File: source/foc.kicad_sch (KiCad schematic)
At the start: 27 parts, among them J1 Conn_01x03, J2 Conn_01x04_Male, J3 Conn_01x05, SW1 SW_DPDT_x2, U1 TJA1050T/CM,118

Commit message: jlcpcb order
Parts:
- added C5, C6: 100n, Capacitor_SMD:C_0603_1608Metric, symbol BLDC_4-rescue:C-RESCUE-BLDC_4
- added H1, H2: MountingHole, MountingHole:MountingHole_2mm, symbol Mechanical:MountingHole
- added R7, R8: 1k, Resistor_SMD:R_0603_1608Metric, symbol BLDC_4-rescue:R-RESCUE-BLDC_4
- added U2: BMI160, Package_LGA:Bosch_LGA-14_3x2.5mm_P0.5mm, symbol Cheap-FOCer-2-60mm-rescue:BMI160-IMU
- renumbered H8 to H10, H9 to H11, H10 to H12, H11 to H13, H12 to H14, H1 to H3, H2 to H4, H3 to H5, H4 to H6, H5 to H7, H6 to H8, H7 to H9
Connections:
- net GND: now also C5.1, C6.1, U2.1 (SDO), U2.6 (GNDIO), U2.7 (GND)
- net VCC: now also C5.2, C6.2, R7.2, R8.1, U2.12 (CSB), U2.5 (VDDIO), U2.8 (VDD)
- new net mcu/PA15: R8.2, U2.13 (SCX)
- new net mcu/PB2: R7.1, U2.14 (SDX)
- no-connect marks 9 -> 15
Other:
- sheet mcu ports: added PA15, PB2; removed none

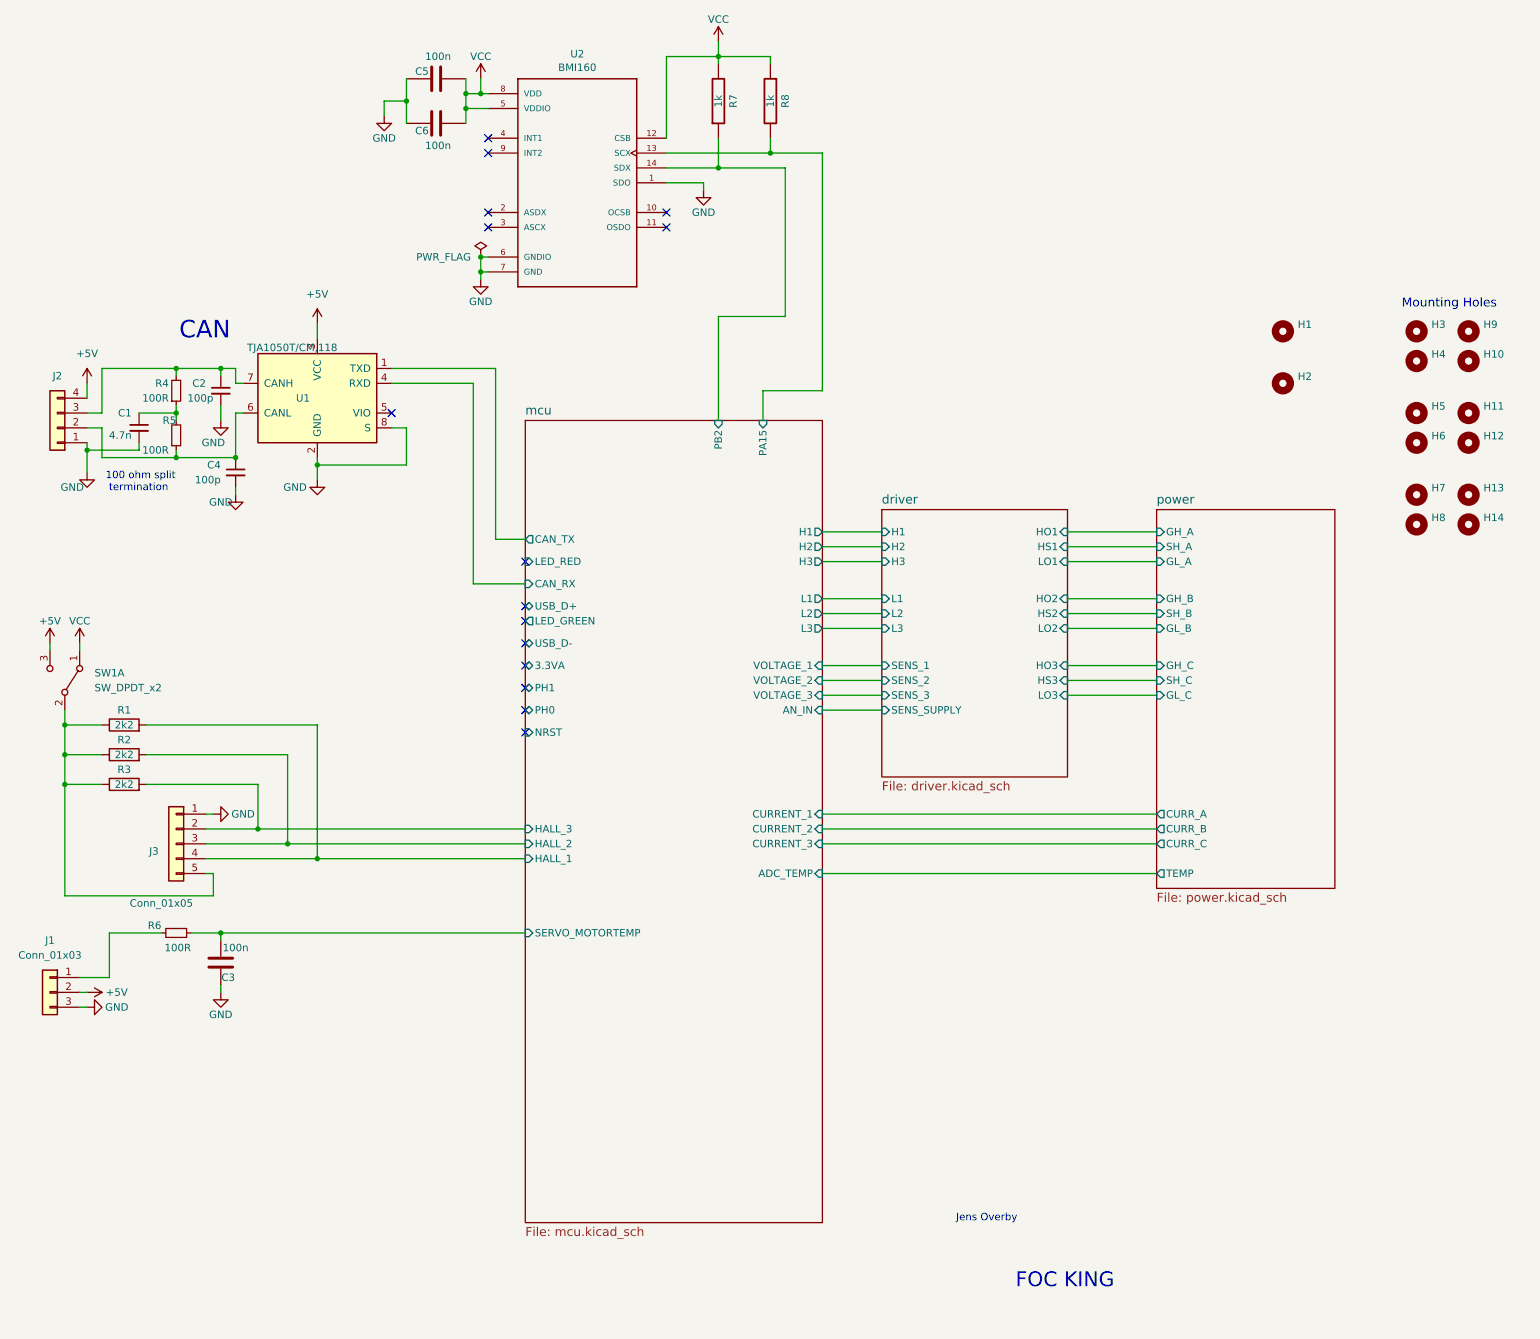
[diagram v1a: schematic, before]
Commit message: jlcpcb reorder of main-module only
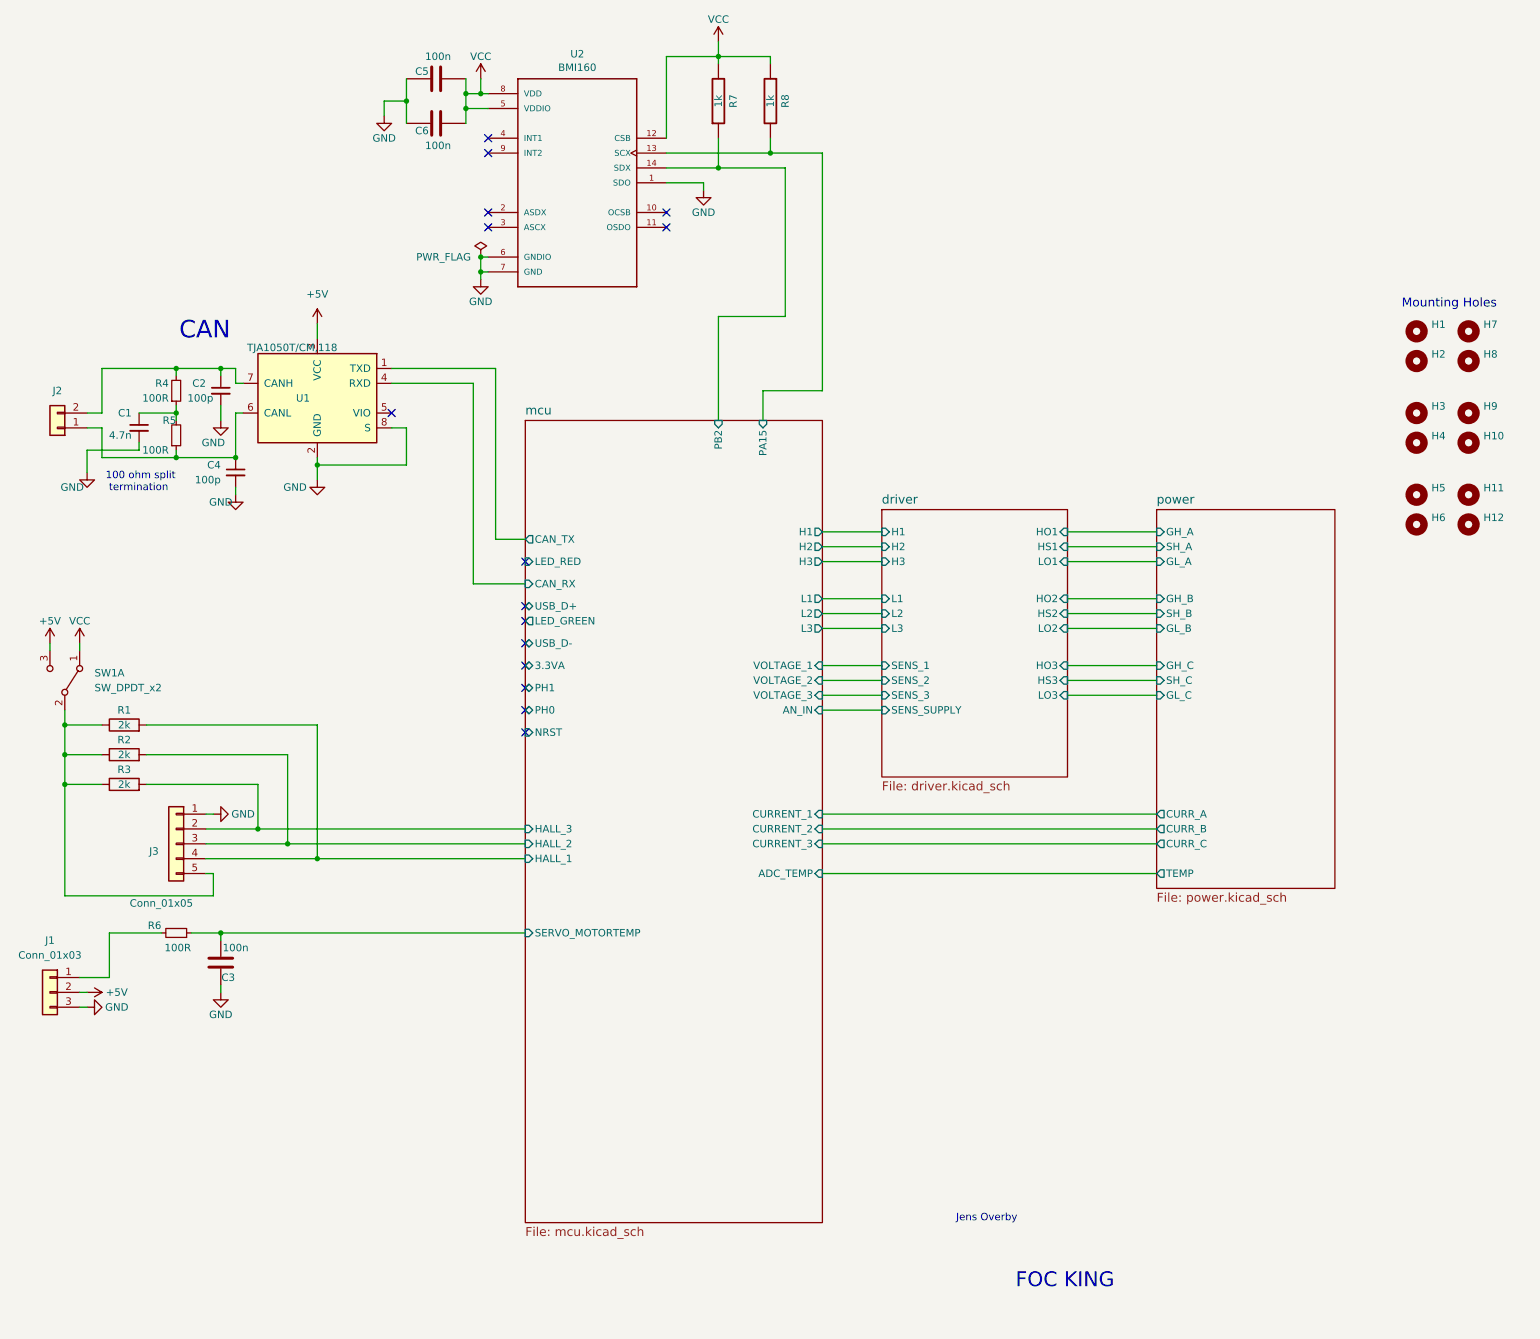
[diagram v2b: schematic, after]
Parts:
- removed H1, H2: MountingHole, MountingHole:MountingHole_2mm, symbol Mechanical:MountingHole
- C3: footprint Resistor_SMD:R_0603_1608Metric -> Capacitor_SMD:C_0603_1608Metric
- J2: footprint Connector_JST:JST_PH_B4B-PH-K_1x04_P2.00mm_Vertical -> Connector_JST:JST_PH_B2B-PH-K_1x02_P2.00mm_Vertical; symbol Connector_Generic:Conn_01x04 -> Connector_Generic:Conn_01x02
- R1, R2, R3: value 2k2 -> 2k
- renumbered H3 to H1, H12 to H10, H13 to H11, H14 to H12, H4 to H2, H5 to H3, H6 to H4, H7 to H5, H8 to H6, H9 to H7, H10 to H8, H11 to H9
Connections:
- net +5V: no longer J2.4 (Pin_4)
- net GND: no longer J2.1 (Pin_1)
- net at C2.1, R4.2, U1.7 (CANH): now also J2.2 (Pin_2); no longer J2.3 (Pin_3)
- net at C4.1, R5.1, U1.6 (CANL): now also J2.1 (Pin_1); no longer J2.2 (Pin_2)

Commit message: Add files via upload
Added six pull down resistors to mosfet gates, and removed 100 pF filter caps on current samplings. Changed Logo back to FOC-king. This is a potential release candidates - everything works, also HFI. Have not yet verified NRF though.
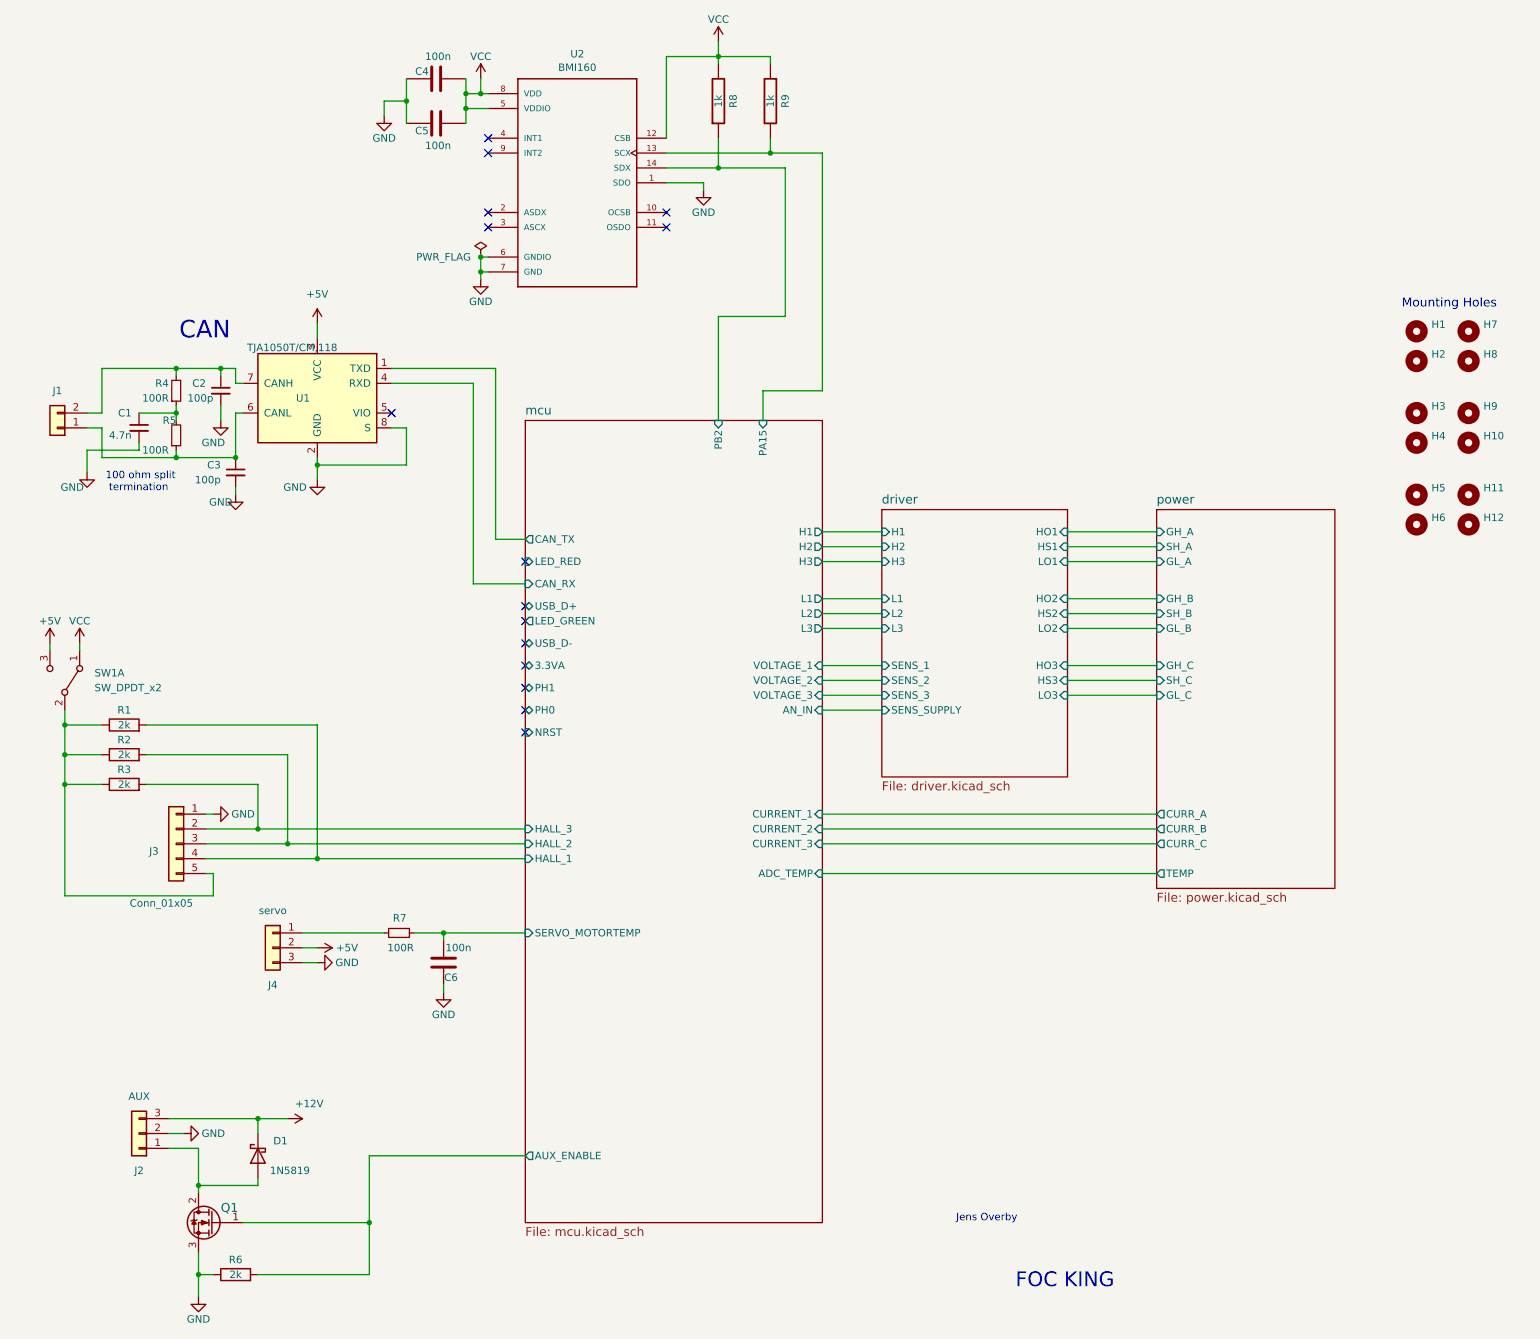
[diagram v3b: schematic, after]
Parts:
- added D1: 1N5819, Diode_SMD:D_SOD-323, symbol Diode:1N5819
- added J2: AUX, Connector_JST:JST_PH_B3B-PH-K_1x03_P2.00mm_Vertical, symbol Connector_Generic:Conn_01x03
- added Q1: AO3400A, Package_TO_SOT_SMD:SOT-23, symbol Device:Q_NMOS_GDS
- added R6: 2k, Resistor_SMD:R_0603_1608Metric, symbol Device:R
- J4: renamed from J1; value Conn_01x03 -> servo
- renumbered C4 to C3, C5 to C4, C6 to C5, C3 to C6, J2 to J1, R6 to R7, R7 to R8, R8 to R9
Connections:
- net GND: now also J2.2 (Pin_2), Q1.3 (S), R6.1
- new net: D1.2 (A), J2.1 (Pin_1), Q1.2 (D)
- new net +12V: D1.1 (K), J2.3 (Pin_3)
- new net mcu/AUX_ENABLE: Q1.1 (G), R6.2
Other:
- sheet mcu ports: added AUX_ENABLE; removed none
- moved on the sheet: C6, J4, R7

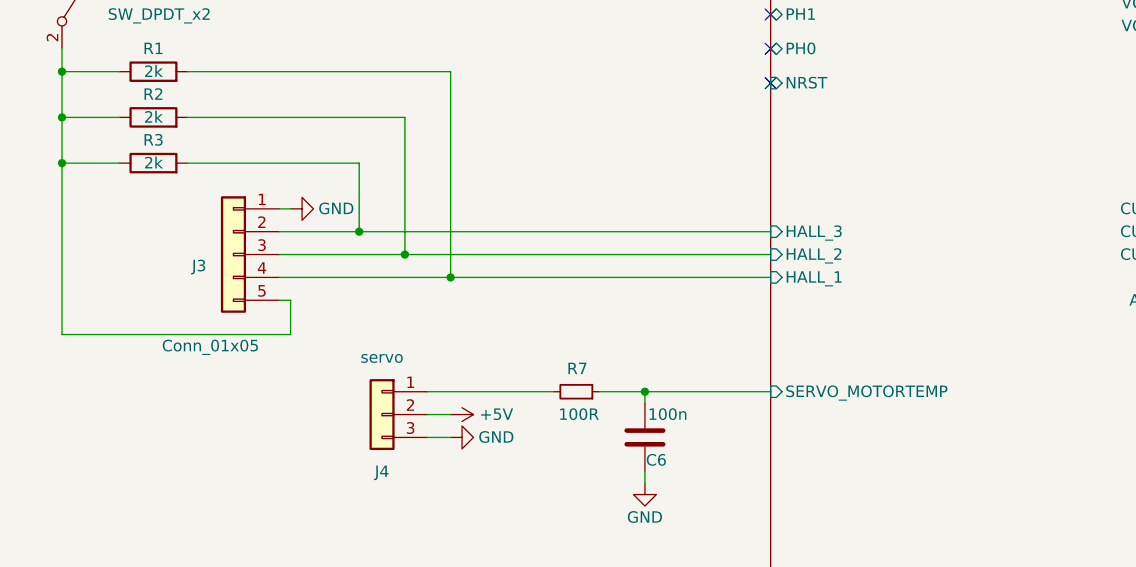
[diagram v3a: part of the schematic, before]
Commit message: Moved traces to make peripherals work
PPM now works -> moved trace to PB7
UART works -> connected PB10 and PB11 to Communication port (like vesc 75_300 UART)
Removed NRF24 pinheader
Added motor_temperature to Hall pinheader, like it should be
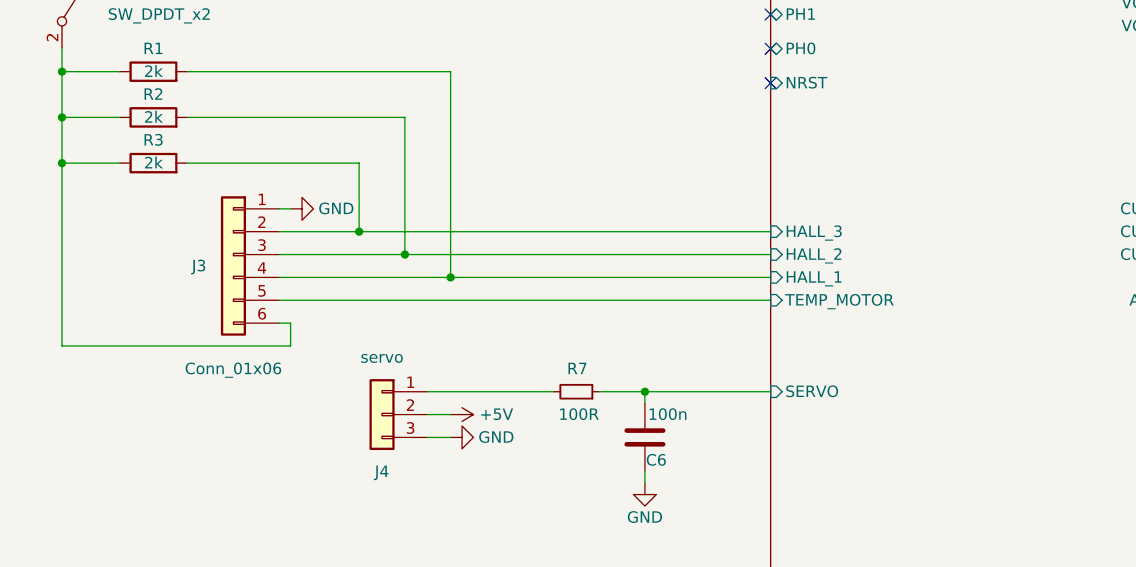
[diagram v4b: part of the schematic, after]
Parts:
- J3: value Conn_01x05 -> Conn_01x06; footprint Connector_JST:JST_PH_B5B-PH-K_1x05_P2.00mm_Vertical -> Connector_JST:JST_PH_B6B-PH-K_1x06_P2.00mm_Vertical; symbol Connector_Generic:Conn_01x05 -> Connector_Generic:Conn_01x06
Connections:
- net at R1.1, R2.1, R3.1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: now also J3.6 (Pin_6); no longer J3.5 (Pin_5)
- net mcu/SERVO_MOTORTEMP renamed mcu/SERVO
- new net mcu/TEMP_MOTOR: J3.5 (Pin_5)
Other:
- sheet mcu ports: added SERVO, TEMP_MOTOR; removed SERVO_MOTORTEMP

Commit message: Add files via upload
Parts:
- added J5: PWR, Connector_JST:JST_XH_B3B-XH-A_1x03_P2.50mm_Vertical, symbol Connector_Generic:Conn_01x03
- added J6: communication, Connector_JST:JST_XH_B7B-XH-A_1x07_P2.50mm_Vertical, symbol Connector_Generic:Conn_01x07
- J1: value Conn_01x04_Male -> Conn_01x02_Male; footprint Connector_JST:JST_PH_B2B-PH-K_1x02_P2.00mm_Vertical -> Connector_JST:JST_XH_B2B-XH-A_1x02_P2.50mm_Vertical
- J4: footprint Connector_JST:JST_PH_B3B-PH-K_1x03_P2.00mm_Vertical -> Connector_JST:JST_XH_B4B-XH-A_1x04_P2.50mm_Vertical; symbol Connector_Generic:Conn_01x03 -> Connector_Generic:Conn_01x04
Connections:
- net +5V: now also J4.3 (Pin_3), J5.1 (Pin_1); no longer J4.2 (Pin_2)
- net GND: now also J4.2 (Pin_2), J5.2 (Pin_2); no longer J4.3 (Pin_3)
- net VCC: now also J4.1 (Pin_1), J5.3 (Pin_3)
- net at R7.2: now also J4.4 (Pin_4); no longer J4.1 (Pin_1)
- new net mcu/ADC_15: J6.7 (Pin_7)
- new net mcu/ADC_8: J6.5 (Pin_5)
- new net mcu/ADC_9: J6.6 (Pin_6)
- new net mcu/MISO_ADC_EXT2: J6.2 (Pin_2)
- new net mcu/RX_SDA_NSS: J6.4 (Pin_4)
- new net mcu/SCK_ADC_EXT: J6.3 (Pin_3)
- new net mcu/TX_SCL_MOSI: J6.1 (Pin_1)
- no-connect marks 15 -> 18
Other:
- sheet mcu ports: added ADC_15, ADC_8, ADC_9, MISO_ADC_EXT2, PC13, PC14, RX_SDA_NSS, SCK_ADC_EXT, SHUTDOWN, TX_SCL_MOSI; removed none

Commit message: Momentary switch
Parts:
- removed C6: 100n, Capacitor_SMD:C_0603_1608Metric, symbol Device:C
- removed D1: 1N5819, Diode_SMD:D_SOD-323, symbol Diode:1N5819
- removed J2: AUX, Connector_JST:JST_PH_B3B-PH-K_1x03_P2.00mm_Vertical, symbol Connector_Generic:Conn_01x03
- removed J4: servo, Connector_JST:JST_XH_B4B-XH-A_1x04_P2.50mm_Vertical, symbol Connector_Generic:Conn_01x04
- removed J5: PWR, Connector_JST:JST_XH_B3B-XH-A_1x03_P2.50mm_Vertical, symbol Connector_Generic:Conn_01x03
- removed J6: communication, Connector_JST:JST_XH_B7B-XH-A_1x07_P2.50mm_Vertical, symbol Connector_Generic:Conn_01x07
- removed Q1: AO3400A, Package_TO_SOT_SMD:SOT-23, symbol Device:Q_NMOS_GDS
- removed R6: 2k, Resistor_SMD:R_0603_1608Metric, symbol Device:R
- removed R7: 100R, Resistor_SMD:R_0603_1608Metric, symbol Device:R_Small
- added C4, C7: 2.2u, Capacitor_SMD:C_0603_1608Metric, symbol Device:C
- added J3: PWR, Connector_JST:JST_XH_B5B-XH-A_1x05_P2.50mm_Vertical, symbol Connector_Generic:Conn_01x05
- added J4: communication, Connector_JST:JST_XH_B6B-XH-A_1x06_P2.50mm_Vertical, symbol Connector_Generic:Conn_01x06
- J2: renamed from J3; footprint Connector_JST:JST_PH_B6B-PH-K_1x06_P2.00mm_Vertical -> Connector_JST:JST_XH_B6B-XH-A_1x06_P2.50mm_Vertical
- U1: value TJA1050T/CM,118 -> TJA1051T/3/1J; LCSC C6952 -> C38695
- renumbered C4 to C5, C5 to C6, R8 to R6, R9 to R7
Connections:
- net +12V: now also J3.4 (Pin_4)
- net +5V: now also C4.1, J3.1 (Pin_1)
- net GND: now also C4.2, C7.2, J3.2 (Pin_2)
- net VCC: now also J3.3 (Pin_3)
- net mcu/ADC_8: now also J4.5 (Pin_5)
- net mcu/ADC_9: now also J4.6 (Pin_6)
- net mcu/LED_RED: now also J3.5 (Pin_5)
- net mcu/MISO_ADC_EXT2: now also J4.2 (Pin_2)
- net mcu/RX_SDA_NSS: now also J4.4 (Pin_4)
- net mcu/SCK_ADC_EXT: now also J4.3 (Pin_3)
- net mcu/TX_SCL_MOSI: now also J4.1 (Pin_1)
- net at U1.5 (VIO): now also C7.1
- no-connect marks 18 -> 16
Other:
- sheet mcu ports: added none; removed ADC_15

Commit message: Add files via upload
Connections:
- net VCC: now also C7.1, U1.5 (VIO)
